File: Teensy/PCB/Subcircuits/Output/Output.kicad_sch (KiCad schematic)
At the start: 5 parts

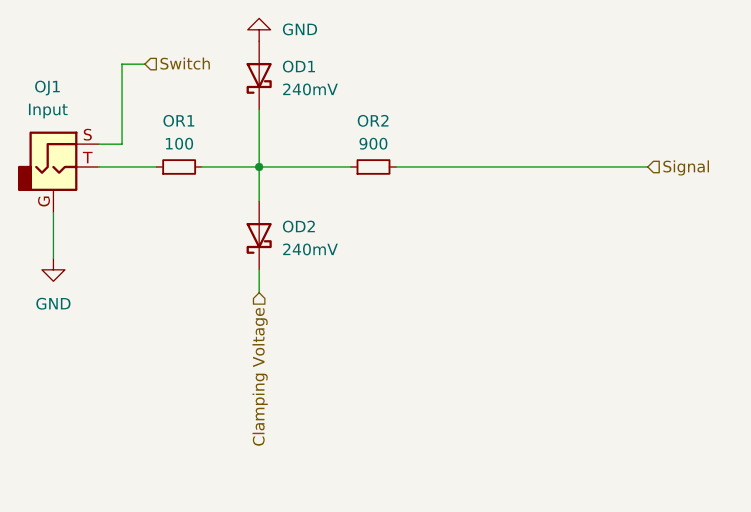
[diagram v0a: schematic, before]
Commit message: Added Panel PCBs
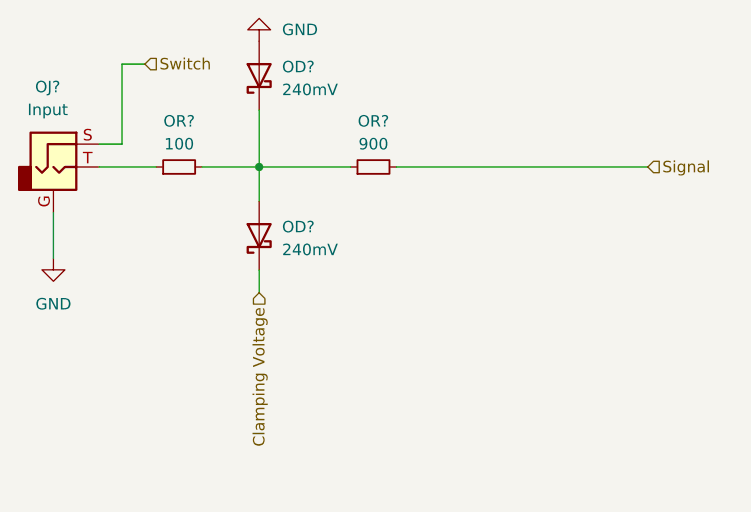
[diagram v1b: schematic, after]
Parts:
- renumbered OD2 to OD?, OD1 to OD?, OJ1 to OJ?, OR1 to OR?, OR2 to OR?
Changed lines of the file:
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@@
   (symbol (lib_id "Device:D_Schottky") (at 102.87 96.52 90) (unit 1)
     (in_bom yes) (on_board yes) (fields_autoplaced)
-    (property "Reference" "OD2" (id 0) (at 105.41 95.5674 90)
+    (property "Reference" "OD?" (id 0) (at 105.41 95.5674 90)
       (effects (font (size 1.27 1.27)) (justify right))
     )
@@
   (symbol (lib_id "Connector:AudioJack2_Ground") (at 80.01 88.9 0) (unit 1)
     (in_bom yes) (on_board yes) (fields_autoplaced)
-    (property "Reference" "OJ1" (id 0) (at 79.375 80.01 0))
+    (property "Reference" "OJ?" (id 0) (at 79.375 80.01 0))
     (property "Value" "Input" (id 1) (at 79.375 82.55 0))
     (property "Footprint" "Perfboard:3.5mm Jack Perfboard" (id 2) (at 80.01 88.9 0)
@@
   (symbol (lib_id "Device:D_Schottky") (at 102.87 78.74 90) (unit 1)
     (in_bom yes) (on_board yes) (fields_autoplaced)
-    (property "Reference" "OD1" (id 0) (at 105.41 77.7874 90)
+    (property "Reference" "OD?" (id 0) (at 105.41 77.7874 90)
       (effects (font (size 1.27 1.27)) (justify right))
     )
@@
   (symbol (lib_id "power:GND") (at 80.01 99.06 0) (unit 1)
     (in_bom yes) (on_board yes) (fields_autoplaced)
-    (property "Reference" "#PWR033" (id 0) (at 80.01 105.41 0)
+    (property "Reference" "#PWR?" (id 0) (at 80.01 105.41 0)
       (effects (font (size 1.27 1.27)) hide)
     )
@@
   (symbol (lib_id "Device:R_Small") (at 93.98 88.9 90) (unit 1)
     (in_bom yes) (on_board yes)
-    (property "Reference" "OR1" (id 0) (at 93.98 83.82 90))
+    (property "Reference" "OR?" (id 0) (at 93.98 83.82 90))
     (property "Value" "100" (id 1) (at 93.98 86.36 90))
     (property "Footprint" "Resistor_SMD:R_1206_3216Metric_Pad1.30x1.75mm_HandSolder" (id 2) (at 93.98 88.9 0)
@@
   (symbol (lib_id "power:GND") (at 102.87 74.93 180) (unit 1)
     (in_bom yes) (on_board yes) (fields_autoplaced)
-    (property "Reference" "#PWR034" (id 0) (at 102.87 68.58 0)
+    (property "Reference" "#PWR?" (id 0) (at 102.87 68.58 0)
       (effects (font (size 1.27 1.27)) hide)
     )
@@
   (symbol (lib_id "Device:R_Small") (at 115.57 88.9 90) (unit 1)
     (in_bom yes) (on_board yes)
-    (property "Reference" "OR2" (id 0) (at 115.57 83.82 90))
+    (property "Reference" "OR?" (id 0) (at 115.57 83.82 90))
     (property "Value" "900" (id 1) (at 115.57 86.36 90))
     (property "Footprint" "Resistor_SMD:R_1206_3216Metric_Pad1.30x1.75mm_HandSolder" (id 2) (at 115.57 88.9 0)

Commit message: Added USB-C Power Supply
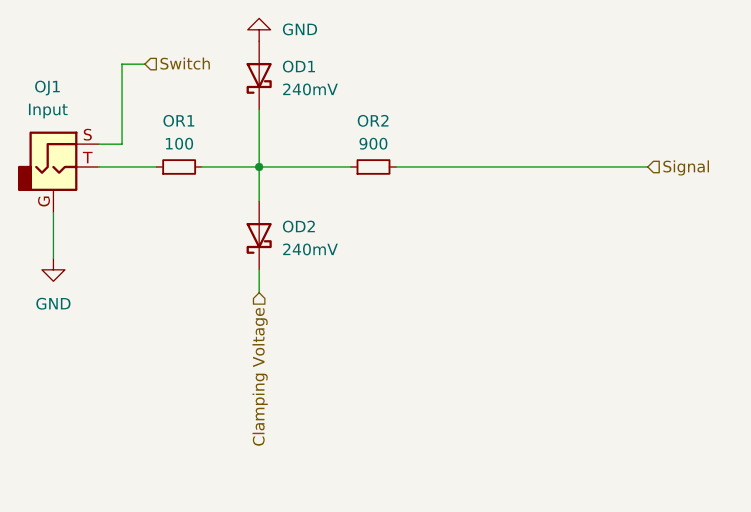
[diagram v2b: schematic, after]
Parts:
- gave numbers to parts that had none: 5
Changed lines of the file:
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@@
   (symbol (lib_id "Device:D_Schottky") (at 102.87 96.52 90) (unit 1)
     (in_bom yes) (on_board yes) (fields_autoplaced)
-    (property "Reference" "OD?" (id 0) (at 105.41 95.5674 90)
+    (property "Reference" "OD2" (id 0) (at 105.41 95.5674 90)
       (effects (font (size 1.27 1.27)) (justify right))
     )
@@
   (symbol (lib_id "Connector:AudioJack2_Ground") (at 80.01 88.9 0) (unit 1)
     (in_bom yes) (on_board yes) (fields_autoplaced)
-    (property "Reference" "OJ?" (id 0) (at 79.375 80.01 0))
+    (property "Reference" "OJ1" (id 0) (at 79.375 80.01 0))
     (property "Value" "Input" (id 1) (at 79.375 82.55 0))
     (property "Footprint" "Perfboard:3.5mm Jack Perfboard" (id 2) (at 80.01 88.9 0)
@@
   (symbol (lib_id "Device:D_Schottky") (at 102.87 78.74 90) (unit 1)
     (in_bom yes) (on_board yes) (fields_autoplaced)
-    (property "Reference" "OD?" (id 0) (at 105.41 77.7874 90)
+    (property "Reference" "OD1" (id 0) (at 105.41 77.7874 90)
       (effects (font (size 1.27 1.27)) (justify right))
     )
@@
   (symbol (lib_id "power:GND") (at 80.01 99.06 0) (unit 1)
     (in_bom yes) (on_board yes) (fields_autoplaced)
-    (property "Reference" "#PWR?" (id 0) (at 80.01 105.41 0)
+    (property "Reference" "#PWR033" (id 0) (at 80.01 105.41 0)
       (effects (font (size 1.27 1.27)) hide)
     )
@@
   (symbol (lib_id "Device:R_Small") (at 93.98 88.9 90) (unit 1)
     (in_bom yes) (on_board yes)
-    (property "Reference" "OR?" (id 0) (at 93.98 83.82 90))
+    (property "Reference" "OR1" (id 0) (at 93.98 83.82 90))
     (property "Value" "100" (id 1) (at 93.98 86.36 90))
     (property "Footprint" "Resistor_SMD:R_1206_3216Metric_Pad1.30x1.75mm_HandSolder" (id 2) (at 93.98 88.9 0)
@@
   (symbol (lib_id "power:GND") (at 102.87 74.93 180) (unit 1)
     (in_bom yes) (on_board yes) (fields_autoplaced)
-    (property "Reference" "#PWR?" (id 0) (at 102.87 68.58 0)
+    (property "Reference" "#PWR034" (id 0) (at 102.87 68.58 0)
       (effects (font (size 1.27 1.27)) hide)
     )
@@
   (symbol (lib_id "Device:R_Small") (at 115.57 88.9 90) (unit 1)
     (in_bom yes) (on_board yes)
-    (property "Reference" "OR?" (id 0) (at 115.57 83.82 90))
+    (property "Reference" "OR2" (id 0) (at 115.57 83.82 90))
     (property "Value" "900" (id 1) (at 115.57 86.36 90))
     (property "Footprint" "Resistor_SMD:R_1206_3216Metric_Pad1.30x1.75mm_HandSolder" (id 2) (at 115.57 88.9 0)
